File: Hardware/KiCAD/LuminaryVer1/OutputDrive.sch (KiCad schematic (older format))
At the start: 6 parts, among them U5 SN65HVD232, U6 SN74LVC07ARGYR

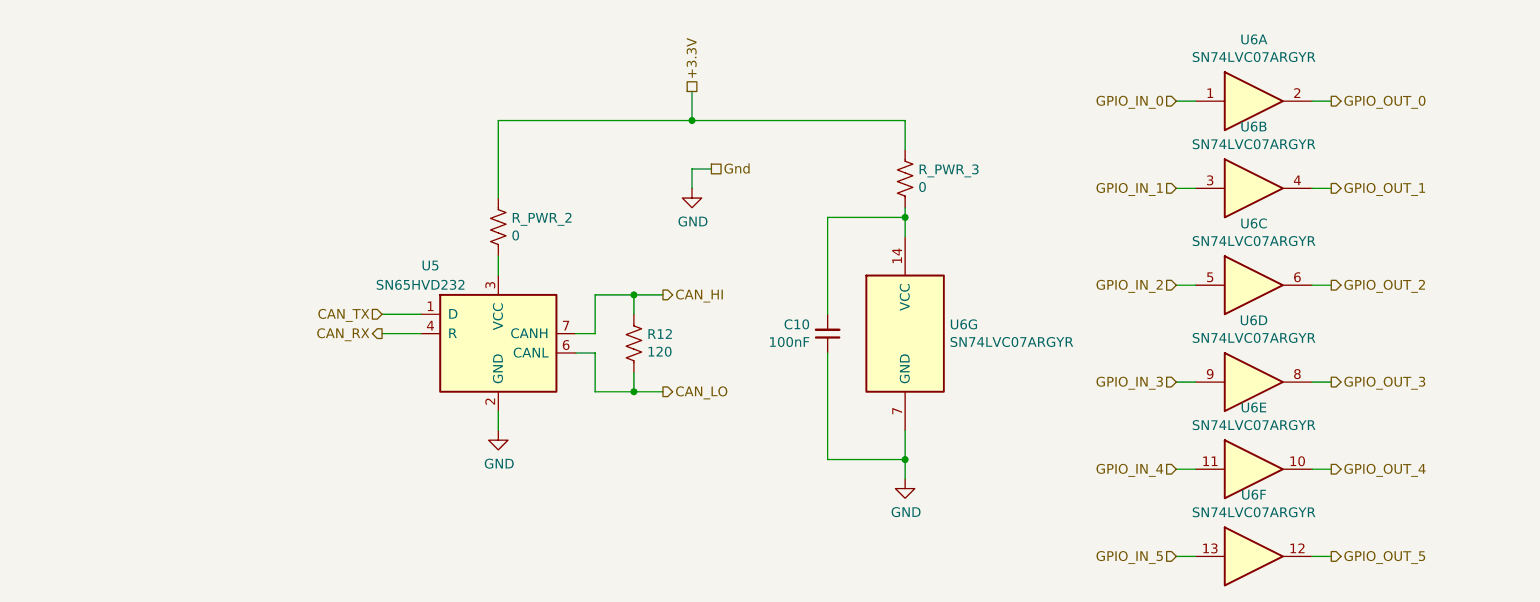
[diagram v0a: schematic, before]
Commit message: Removed GPIO output driver to increase versatility as IO. Added passive over-current/voltage protection.
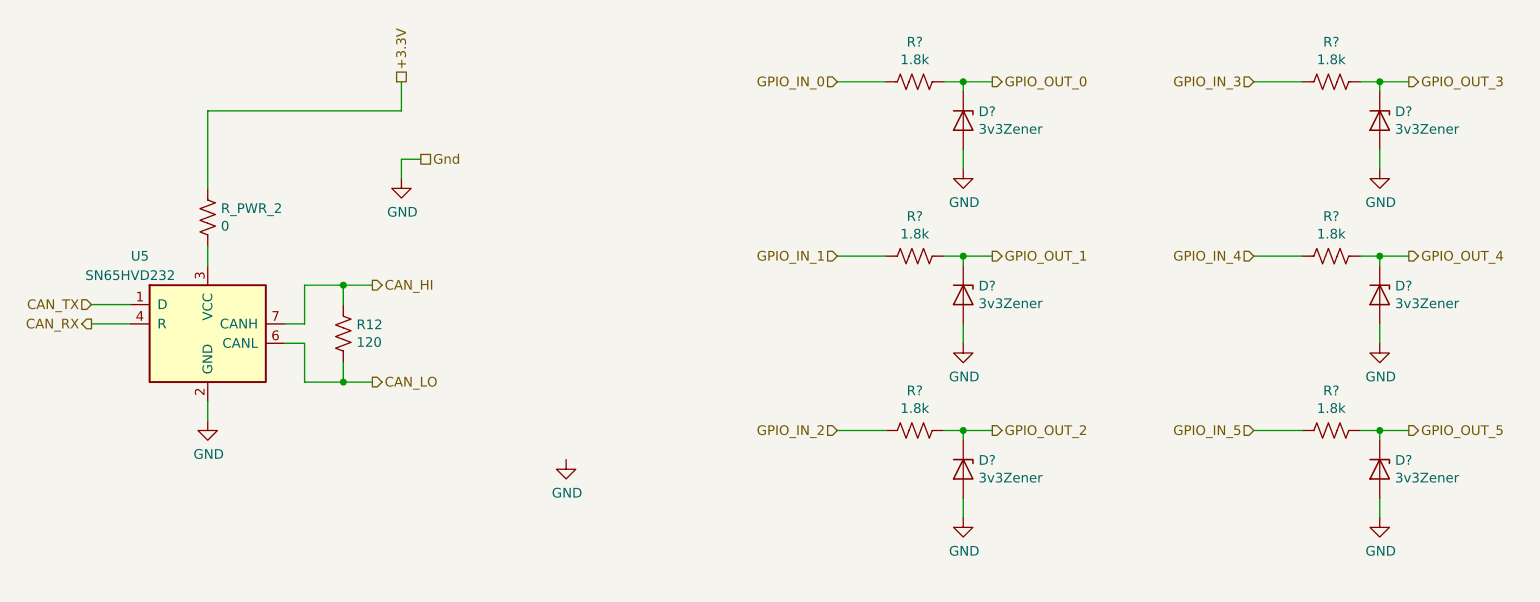
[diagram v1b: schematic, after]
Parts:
- removed C10: 100nF, symbol Device:C_Small
- removed R_PWR_3: 0, symbol Device:R_US
- removed U6: SN74LVC07ARGYR, symbol 74xx:74LCX07
- added D? (x6): 3v3Zener, symbol Device:D_Zener
- added R? (x6): 1.8k, symbol Device:R_US
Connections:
- net GND: now also D?.2 (A), D?.2 (A), D?.2 (A), D?.2 (A), D?.2 (A), D?.2 (A)
- net GPIO_IN_0: now also R?.2
- net GPIO_IN_1: now also R?.2
- net GPIO_IN_2: now also R?.2
- net GPIO_IN_3: now also R?.2
- net GPIO_IN_4: now also R?.2
- net GPIO_IN_5: now also R?.2
- net GPIO_OUT_0: now also D?.1 (K), R?.1
- net GPIO_OUT_1: now also D?.1 (K), R?.1
- net GPIO_OUT_2: now also D?.1 (K), R?.1
- net GPIO_OUT_3: now also D?.1 (K), R?.1
- net GPIO_OUT_4: now also D?.1 (K), R?.1
- net GPIO_OUT_5: now also D?.1 (K), R?.1
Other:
- moved on the sheet: R12, R_PWR_2, U5
